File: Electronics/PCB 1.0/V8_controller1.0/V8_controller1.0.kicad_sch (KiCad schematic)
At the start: 11 parts, among them Q1 IRLZ34N, SW1 SW_SPST, U1 LM317_TO-263

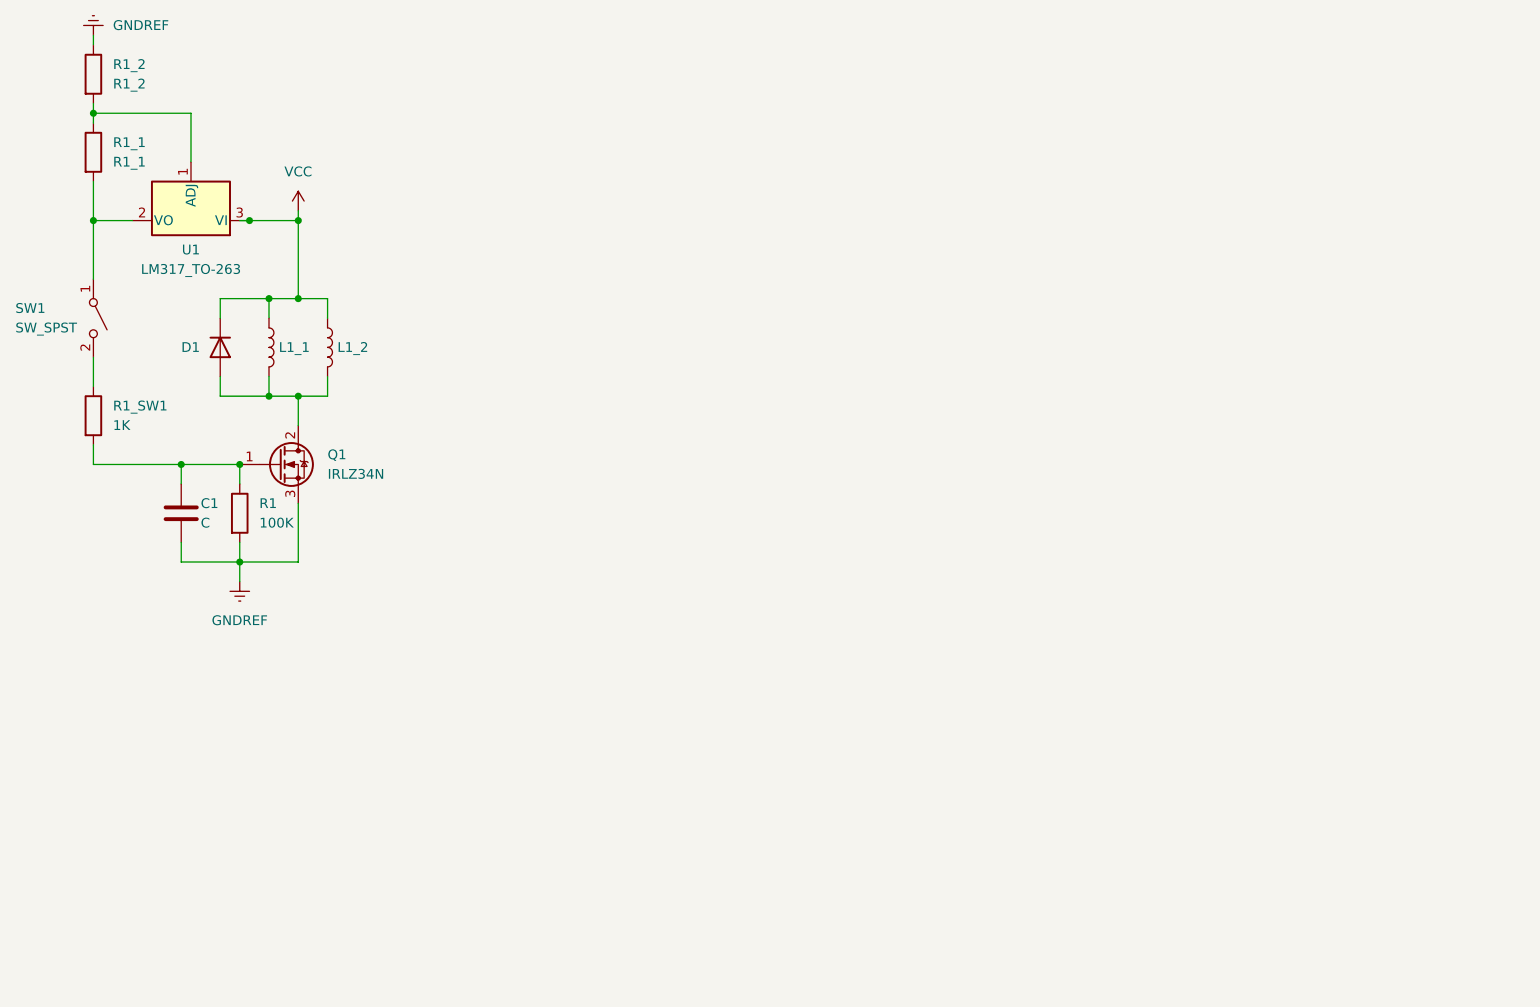
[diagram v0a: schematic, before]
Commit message: Add voltage control with extra LM317
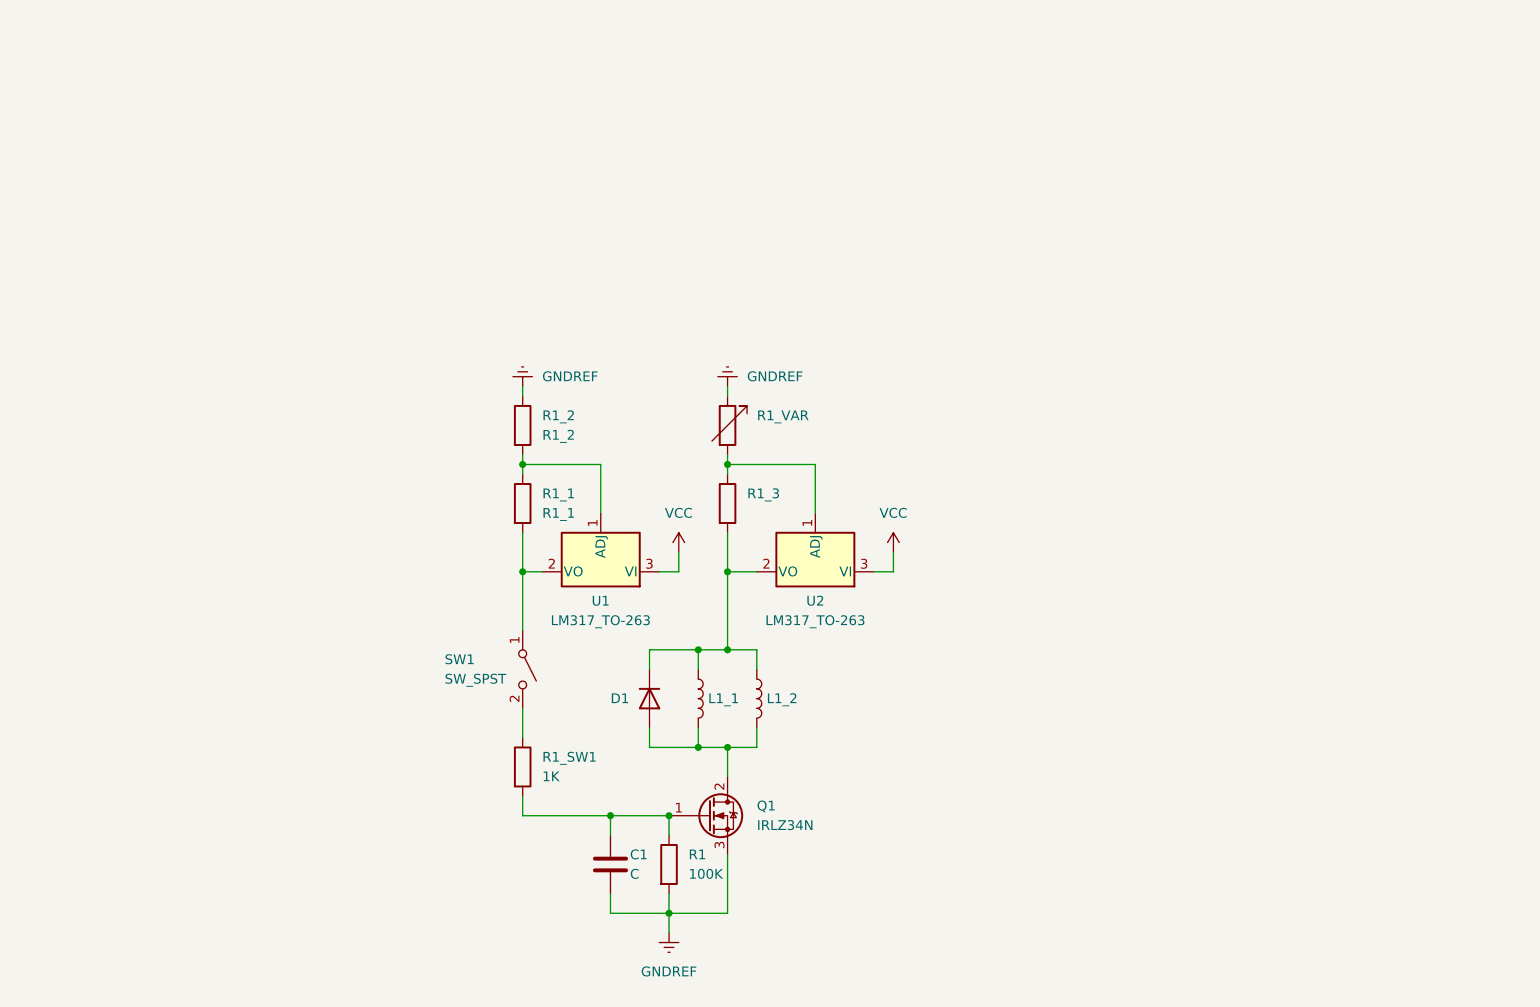
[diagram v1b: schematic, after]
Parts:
- added R1_3: (no value), Resistor_SMD:R_0805_2012Metric_Pad1.20x1.40mm_HandSolder, symbol Device:R
- added R1_VAR: (no value), symbol Device:R_Variable
- added U2: LM317_TO-263, Package_TO_SOT_SMD:TO-263-2, symbol Regulator_Linear:LM317_TO-263
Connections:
- net GNDREF: now also R1_VAR.1
- net VCC: now also U2.3 (VI); no longer D1.2 (K), L1_1.1, L1_2.1
- new net: D1.2 (K), L1_1.1, L1_2.1, R1_3.2, U2.2 (VO)
- new net: R1_3.1, R1_VAR.2, U2.1 (ADJ)
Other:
- moved on the sheet: C1, D1, L1_1, L1_2, Q1, R1, R1_1, R1_2, R1_SW1, SW1, U1

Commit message: Add final gerberfiles for 1.0
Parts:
- removed R1_1: R1_1, Resistor_SMD:R_0805_2012Metric_Pad1.20x1.40mm_HandSolder, symbol Device:R
- removed R1_2: R1_2, Resistor_SMD:R_0805_2012Metric_Pad1.20x1.40mm_HandSolder, symbol Device:R
- removed U1: LM317_TO-263, Package_TO_SOT_SMD:TO-263-2, symbol Regulator_Linear:LM317_TO-263
- added C2: C, Resistor_SMD:R_0805_2012Metric_Pad1.20x1.40mm_HandSolder, symbol Device:C
- added D2: DIODE, Diode_SMD:D_SMA-SMB_Universal_Handsoldering, symbol Simulation_SPICE:DIODE
- added J1: VCC 4mm banana CT3151, Connector:CalTest_CT3151, symbol Connector:Conn_01x01_Female
- added J2: GND 4mm banana CT3151, Connector:CalTest_CT3151, symbol Connector:Conn_01x01_Female
- added L2_1, L2_2: L, Connector_JST:JST_EH_S2B-EH_1x02_P2.50mm_Horizontal, symbol Device:L
- added Q2: IRLZ34N, Package_TO_SOT_THT:TO-220-3_Horizontal_TabDown, symbol Transistor_FET:IRLZ34N
- added R2: 100K, Resistor_SMD:R_0805_2012Metric_Pad1.20x1.40mm_HandSolder, symbol Device:R
- added R2_SW1: 1K, Resistor_SMD:R_0805_2012Metric_Pad1.20x1.40mm_HandSolder, symbol Device:R
- added R3_1: R1_1, Resistor_SMD:R_0805_2012Metric_Pad1.20x1.40mm_HandSolder, symbol Device:R
- added R3_2: R3_2, Resistor_SMD:R_0805_2012Metric_Pad1.20x1.40mm_HandSolder, symbol Device:R
- added SW2: SW_SPST, Connector_JST:JST_EH_S2B-EH_1x02_P2.50mm_Horizontal, symbol Switch:SW_SPST
- added U3: LM317, Package_TO_SOT_SMD:TO-263-2, symbol Regulator_Linear:LM317_TO-263
- R1_3: value (none) -> R1_3
- R1_VAR1: renamed from R1_VAR; value (none) -> R_Variable; footprint (none) -> Resistor_THT:R_Axial_DIN0204_L3.6mm_D1.6mm_P1.90mm_Vertical
- U1_2: renamed from U2; value LM317_TO-263 -> LM338; footprint Package_TO_SOT_SMD:TO-263-2 -> Package_TO_SOT_THT:TO-220-3_Horizontal_TabDown
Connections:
- net GNDREF: now also C2.2, J2.1 (Pin_1), Q2.3 (S), R2.2, R3_2.1
- net VCC: now also J1.1 (Pin_1), U3.3 (VI)
- net Vdrive: now reaches D1.2 (K), L1_1.1, L1_2.1, R1_3.2, U1_2.2 (VO)
- net Vdrive: now also D2.2 (K), L2_1.1, L2_2.1
- net VCOM: now reaches SW1.1 (A)
- net VCOM: now also R3_1.2, SW2.1 (A), U3.2 (VO)
- new net: C2.1, Q2.1 (G), R2.1, R2_SW1.2
- new net: D2.1 (A), L2_1.2, L2_2.2, Q2.2 (D)
- new net: R2_SW1.1, SW2.2 (B)
- new net: R3_1.1, R3_2.2, U3.1 (ADJ)
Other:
- moved on the sheet: C1, D1, L1_1, L1_2, Q1, R1, R1_3, R1_SW1, R1_VAR1, SW1, U1_2
